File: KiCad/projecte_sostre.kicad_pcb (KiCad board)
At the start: 2 copper layers, 111.2 x 89.4 mm, 149 parts, among them J1 Conn_01x02, J10 DE9_Pins, J11 DE9_Pins, J2 Conn_01x05, J3 Conn_01x02, J4 Conn_01x02, J5 Conn_01x02, J6 Conn_01x02, J7 Screw_Terminal_01x02, J8 Screw_Terminal_01x02, J9 Screw_Terminal_01x02, SW1 SW_Push, SW2 SW_Push, SW3 SW_Push, SW4 SW_Push, SW5 SW_Push, SW6 SW_Push, U1 74AHCT1G125, U10 MCP2561-E-MF, U11 MAX3232, U12 A1101xLH, U13 A1101xLH, U14 L298P, U2 LM393, U3 LM393, U4 PIC24HJ128GP502, U5 LM1117DT-3.3, U6 LM2596T-5, U8 INA219AxD, U9 INA219AxD, Y1 Crystal

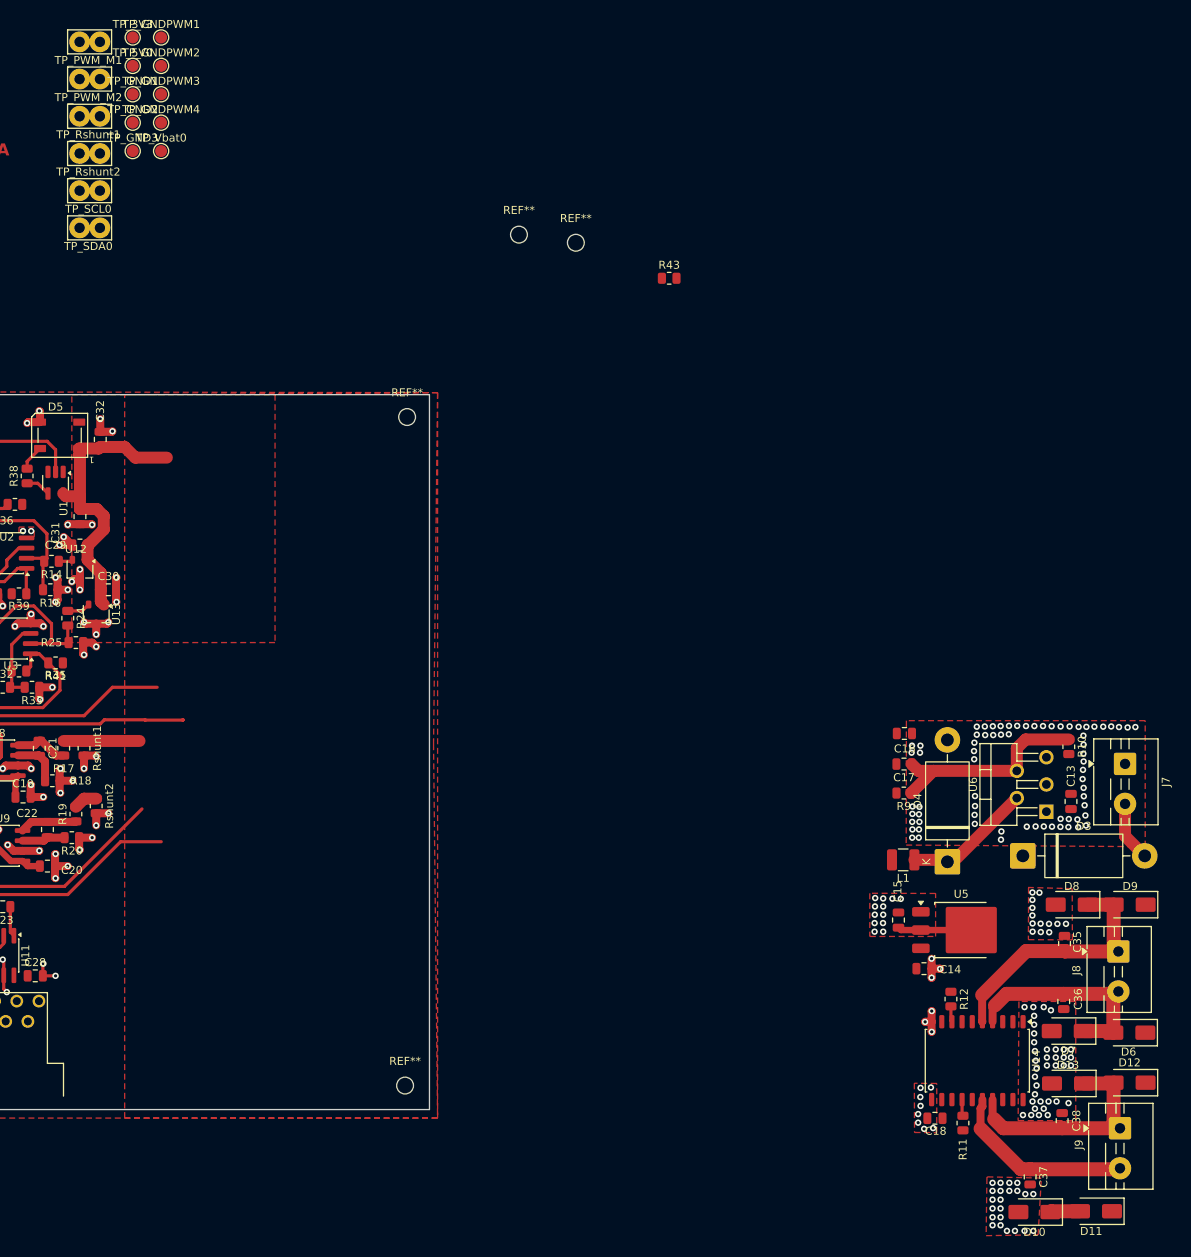
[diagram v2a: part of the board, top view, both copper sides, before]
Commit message: Voy a intentar mejorar el LED, sensor hall / sensor antiatrapamiento
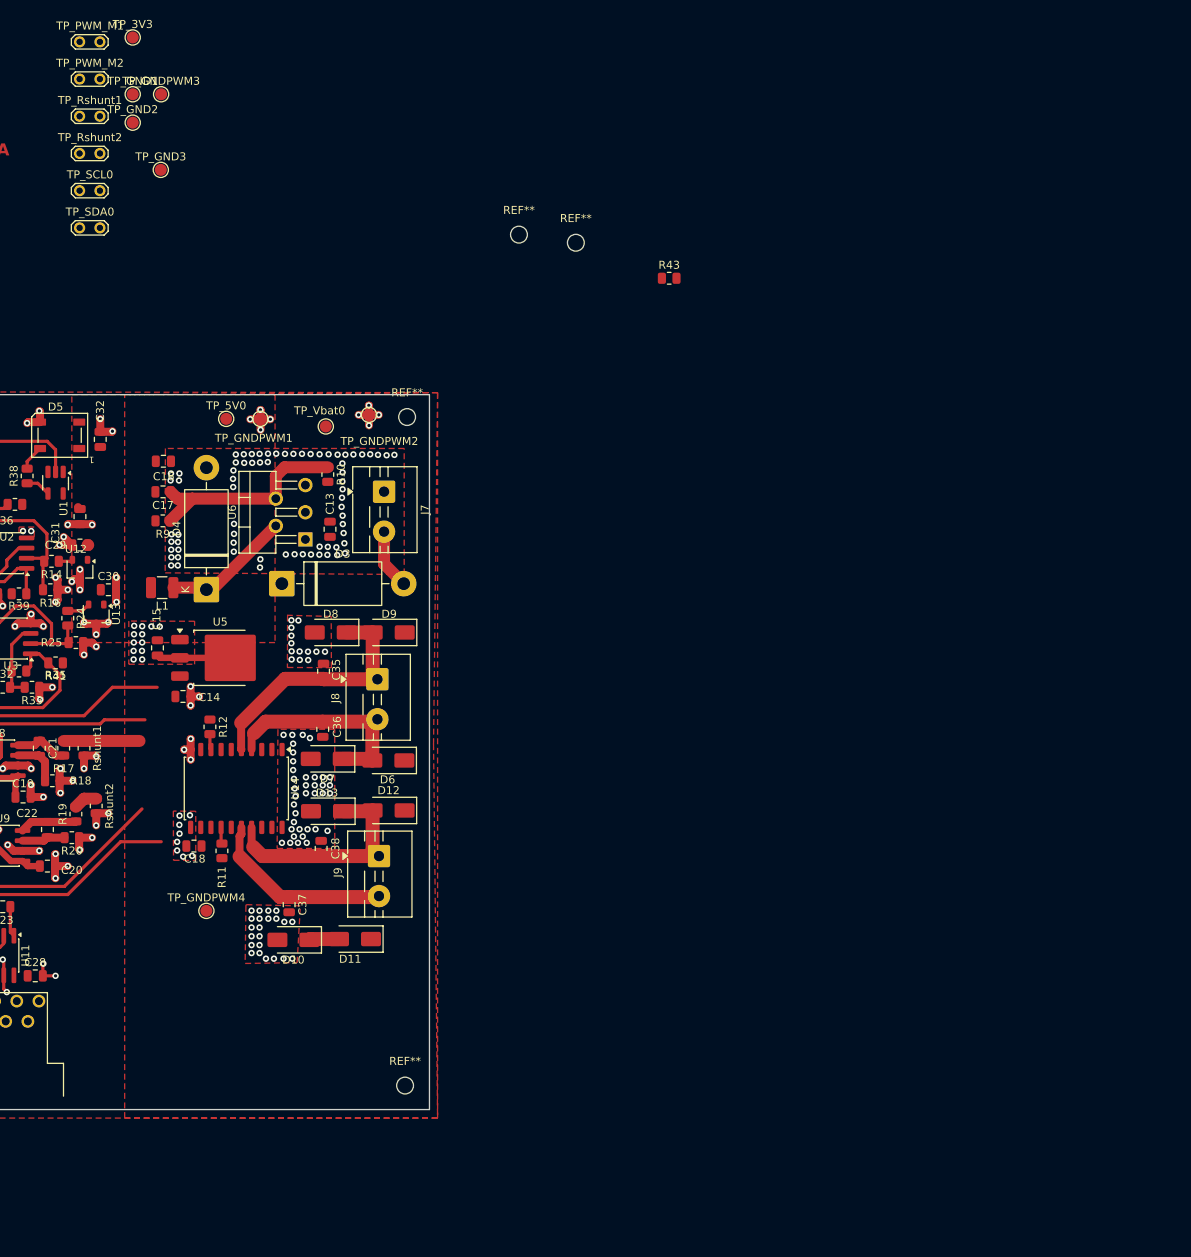
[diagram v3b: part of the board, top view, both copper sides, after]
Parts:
- TP_PWM_M1, TP_PWM_M2, TP_Rshunt1, TP_Rshunt2, TP_SCL0, TP_SDA0: footprint TestPoint:TestPoint_Bridge_Pitch2.54mm_Drill1.3mm -> TestPoint:TestPoint_2Pads_Pitch2.54mm_Drill0.8mm
- moved TP_GNDPWM4 98.7 mm to (213.9, 125.0)
- moved D3 98.7 mm to (223.4, 84.1)
- moved D6 98.7 mm to (236.7, 106.2)
- moved R10 98.7 mm to (229.1, 70.4)
- moved R9 98.7 mm to (208.5, 76.2)
- moved U14 98.7 mm to (217.7, 109.7)
- moved C13 98.7 mm to (229.4, 77.3)
- moved C14 98.7 mm to (211.0, 98.2)
- moved C15 98.7 mm to (207.8, 92.1)
- moved C16 98.7 mm to (208.6, 68.8)
- moved C17 98.7 mm to (208.5, 72.6)
- moved C18 98.7 mm to (212.4, 116.9)
- moved C35 98.7 mm to (228.6, 95.0)
- moved D10 98.7 mm to (224.8, 128.6)
- moved D11 98.7 mm to (232.5, 128.5)
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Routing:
- net 5V: track 37.9 -> 0.43 mm
- net GND: track 154.5 -> 164.6 mm, vias 318 -> 326
- net INA1_M1: track 56.3 -> 51.5 mm

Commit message: ultimos cambios, he puesto abajo sensor anti atrapamiento (usa AVDD y SENSOR_A y _B PROBLEMA porque atraviesa todo una linea muy ancha
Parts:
- moved TP_Rshunt2 110.5 mm to (230.8, 135.8)
- moved TP_Rshunt1 102.7 mm to (209.4, 127.8), turned to 180 degrees
- moved C32 84.8 mm to (281.4, 91.8)
- moved C33 84.8 mm to (267.7, 111.1)
- moved R14 84.8 mm to (275.3, 107.0)
- moved R25 84.8 mm to (278.4, 117.2)
- moved R26 84.8 mm to (264.7, 103.6)
- moved R32 84.8 mm to (269.2, 122.8)
- moved R36 84.8 mm to (270.8, 99.9)
- moved R38 84.8 mm to (272.3, 96.4)
- moved R40 84.8 mm to (264.7, 107.6)
- moved C29 84.8 mm to (278.9, 105.0)
- moved C30 84.8 mm to (282.4, 110.6)
- moved C31 84.8 mm to (278.9, 101.5)
- moved C34 84.8 mm to (266.7, 120.8)
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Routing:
- net SENSE_B: track 2.96 -> 56.4 mm
- net SENSE_A: track 9.48 -> 57.6 mm
- net I2C_SCL: track 70.4 -> 93.1 mm
- net I2C_SDA: track 76.1 -> 97.0 mm
- net GND: track 164.6 -> 182.0 mm, vias 326 -> 366
- net /Analogica/IN+: track 13.9 -> 30.7 mm
- net /Analogica/IN-: track 11.6 -> 23.3 mm
- net INB2_M2: track 58.8 -> 51.0 mm, vias 0 -> 2
- net M2_OUT1: track 27.1 -> 34.2 mm
- net AVDD: track 59.1 -> 66.0 mm, vias 0 -> 2
- net INB1_M2: track 61.9 -> 62.7 mm, vias 0 -> 2
- added copper zone on F.Cu, net AVDD
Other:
- board text added: "mirar TEMA 3V3 y pq no llega, hacer que llegue poniendo algo"

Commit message: Sensor Hall y LED mas o menos definitivos
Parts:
- moved R39 102.1 mm to (175.0, 77.2)
- moved R33 91.8 mm to (189.3, 84.8)
- moved R32 91.7 mm to (185.9, 84.5)
- moved U2 89.8 mm to (184.2, 78.8), turned to 0 degrees
- moved R42 89.8 mm to (179.2, 88.4), turned to -90 degrees
- moved R30 88.4 mm to (175.0, 79.7)
- moved R34 87.8 mm to (179.1, 77.9), turned to 90 degrees
- moved R25 87.4 mm to (194.7, 92.2)
- moved C33 87.3 mm to (188.3, 74.9)
- moved R24 87.2 mm to (193.8, 89.1)
- moved R14 87.1 mm to (193.7, 76.7), turned to -90 degrees
- moved C34 87.1 mm to (184.2, 92.7)
- moved U3 87.1 mm to (187.8, 88.8)
- moved U12 86.8 mm to (197.9, 76.8)
- moved R16 86.6 mm to (194.3, 79.5)
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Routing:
- net GND: track 182.0 -> 88.2 mm, vias 366 -> 381
- net AVDD: track 66.0 -> 39.0 mm
- net LED_RGB: track 72.9 -> 46.9 mm
- net HIGH_UP_M1_Pos_Max: track 69.5 -> 45.8 mm
- net I2C_SDA: track 97.0 -> 75.6 mm
- net /Digital/VOUT_Hall2: track 31.6 -> 15.5 mm
- net DOWN_LOW_M1_Pos_Min: track 49.6 -> 34.4 mm, vias 0 -> 2
- net I2C_SCL: track 93.1 -> 78.1 mm, vias 4 -> 2
- net DOWN_LOW_M1_Pos_Max: track 41.6 -> 27.4 mm
- net /Analogica/IN+: track 30.7 -> 16.8 mm
- net /Analogica/IN-: track 23.3 -> 11.7 mm
- net SENSE_A: track 57.6 -> 48.1 mm
- net INB1_M2: track 62.7 -> 53.3 mm
- net /Digital/Vref_1V_Max: track 18.0 -> 8.88 mm
- net +3.3V: track 14.5 -> 21.0 mm
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
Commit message: Layout con pocos cables en capa Bot pero todavai hay que hacer cambios que nos dijo el Miercoles pasado
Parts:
- removed TP_GNDPWM3: TestPoint, TestPoint:TestPoint_Pad_D1.5mm
- R43: moved to B.Cu
- moved REF** 184.2 mm to (108.3, 145.8)
- moved REF** 146.1 mm to (108.2, 60.0)
- moved TP_SDA0 110.4 mm to (157.7, 142.4)
- moved TP_SCL0 109.3 mm to (157.7, 136.5)
- moved TP_GND2 101.8 mm to (140.1, 105.1)
- moved R43 97.9 mm to (185.4, 92.1), turned to -90 degrees
- moved TP_PWM_M2 86.5 mm to (178.3, 105.2)
- moved TP_3V3 86.0 mm to (139.0, 71.3)
- moved TP_PWM_M1 85.3 mm to (167.9, 96.1)
- moved TP_GND1 84.5 mm to (135.5, 71.4)
- moved J5 78.4 mm to (109.0, 94.5)
- moved J3 74.4 mm to (109.0, 74.2), turned to 0 degrees
- moved SW4 73.1 mm to (112.5, 88.5), turned to 90 degrees
- moved J6 73.0 mm to (109.1, 104.7), turned to 0 degrees
- moved SW5 72.4 mm to (112.6, 98.5), turned to 90 degrees
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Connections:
- TP_PWM_M1 pad 1: INA1_M1 -> INA2_M1
- U4 pad 10: INB1_M2 -> CAN_TX
- U4 pad 11: INB2_M2 -> STBY_Trans_CAN
- U4 pad 14: unconnected-(U4-RB14-Pad14) -> USART_TX
- U4 pad 15: unconnected-(U4-RB15-Pad15) -> USART_RX
- U4 pad 2: unconnected-(U4-RC6-Pad2) -> /Microprocesador/M1_go_Max
- U4 pad 23: INA1_M1 -> uC_programado?
- U4 pad 24: INA2_M1 -> unconnected-(U4-RB3-Pad24)
- U4 pad 25: DOWN_LOW_M1_Pos_Min -> unconnected-(U4-RC0-Pad25)
- U4 pad 26: HIGH_UP_M1_Pos_Min -> INB1_M2
- U4 pad 27: DOWN_LOW_M1_Pos_Max -> INB2_M2
- U4 pad 3: uC_programado? -> /Microprocesador/M1_go_Min
- U4 pad 32: HIGH_UP_M1_Pos_Max -> INA1_M1
- U4 pad 33: LED_RGB -> INA2_M1
- U4 pad 34: STBY_Trans_CAN -> DOWN_LOW_M1_Pos_Min
- U4 pad 35: ON/OFF_LED -> HIGH_UP_M1_Pos_Min
- U4 pad 36: CAN_RX -> unconnected-(U4-RC3-Pad36)
- U4 pad 37: CAN_TX -> unconnected-(U4-RC4-Pad37)
- U4 pad 38: /Microprocesador/M1_go_Max -> unconnected-(U4-RC5-Pad38)
- U4 pad 4: unconnected-(U4-RC8-Pad4) -> /Microprocesador/M2_go_Max
- U4 pad 41: /Microprocesador/M1_go_Min -> DOWN_LOW_M1_Pos_Max
- U4 pad 42: /Microprocesador/M2_go_Max -> HIGH_UP_M1_Pos_Max
- U4 pad 43: /Microprocesador/M2_go_Min -> LED_RGB
- U4 pad 5: unconnected-(U4-RC9-Pad5) -> /Microprocesador/M2_go_Min
- U4 pad 8: USART_TX -> ON/OFF_LED
- U4 pad 9: USART_RX -> CAN_RX
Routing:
- net I2C_SDA: track 75.6 -> 131.3 mm, vias 2 -> 4
- net I2C_SCL: track 78.1 -> 130.0 mm, vias 2 -> 4
- net /Microprocesador/M1_go_Max: track 15.7 -> 63.2 mm, vias 1 -> 0
- net +3.3V: track 21.0 -> 68.0 mm, vias 0 -> 14
- net /Microprocesador/M1_go_Min: track 14.1 -> 56.2 mm
- net AVDD: track 39.0 -> 77.4 mm, vias 2 -> 6
- net (no net): track 36.8 -> 0.00 mm
- net STBY_Trans_CAN: track 4.18 -> 40.2 mm, vias 1 -> 0
- net CAN_TX: track 3.05 -> 32.5 mm
- net LED_RGB: track 46.9 -> 76.2 mm
- net CAN_RX: track 2.83 -> 30.6 mm
- net HIGH_UP_M1_Pos_Min: track 6.24 -> 27.0 mm
- net ON/OFF_LED: track 20.2 -> 40.9 mm, vias 1 -> 0
- net DOWN_LOW_M1_Pos_Max: track 27.4 -> 45.7 mm
- net INA2_M1: track 52.2 -> 33.9 mm
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- added copper zone on B.Cu, net GND
- removed copper zone on F.Cu, net (none)
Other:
- board size 111.2 x 89.4 mm -> 111.8 x 92.1 mm
- board text added: "Fet per: Marc Baillo i Nabel Khrourouch"
- board text removed: "3V3 o 5V"
- board text removed: "ACORDARSE PONER TEST EN LA PCB"
- board text removed: "GND Power"
- board text removed: "GND normal"
- board text removed: "mirar TEMA 3V3 y pq no llega, hacer que llegue poniendo algo"
- board text removed: "señales digitales"

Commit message: Cambios Layout propuestos para mejorar posicionamiento
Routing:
- net +3.3V: track 68.0 -> 57.2 mm
- net GND: track 83.1 -> 79.0 mm
- net AVDD: track 77.4 -> 78.8 mm, vias 6 -> 7

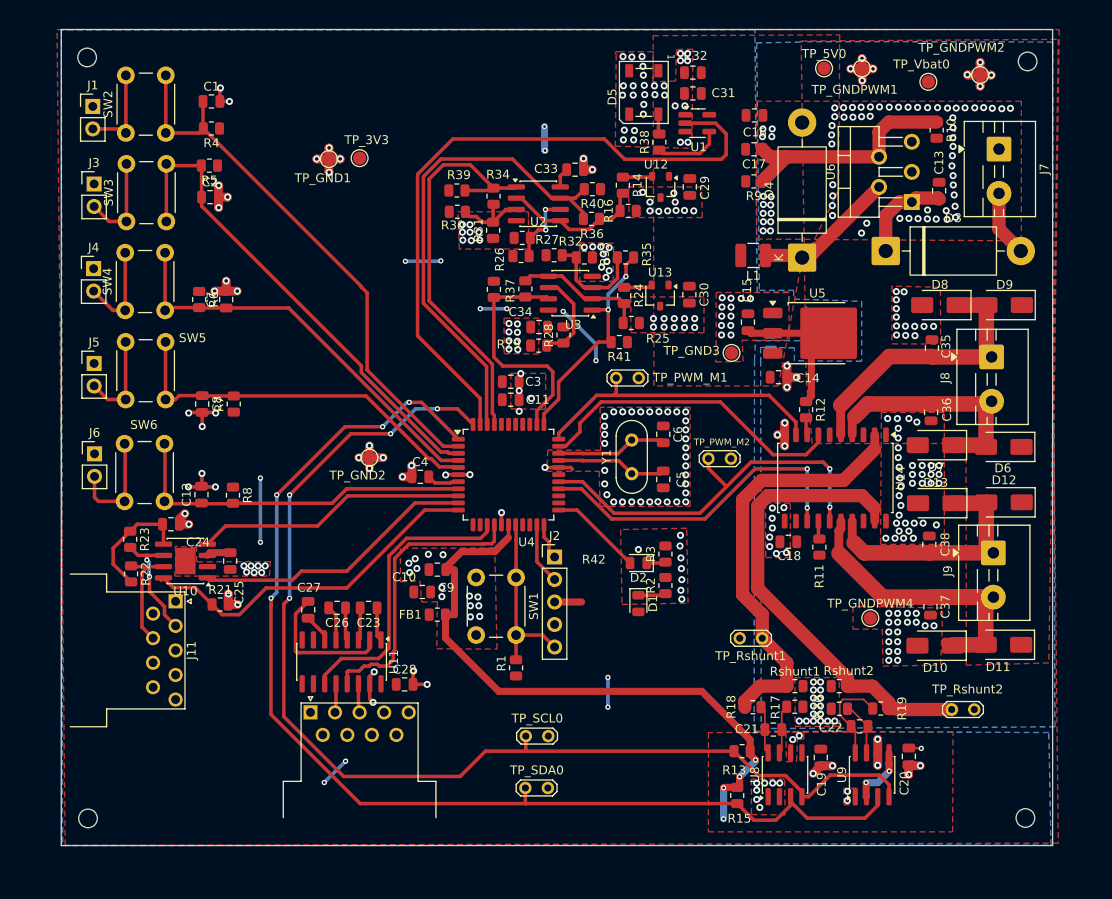
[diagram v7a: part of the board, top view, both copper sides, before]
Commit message: Arreglo de algunos fallos DRC
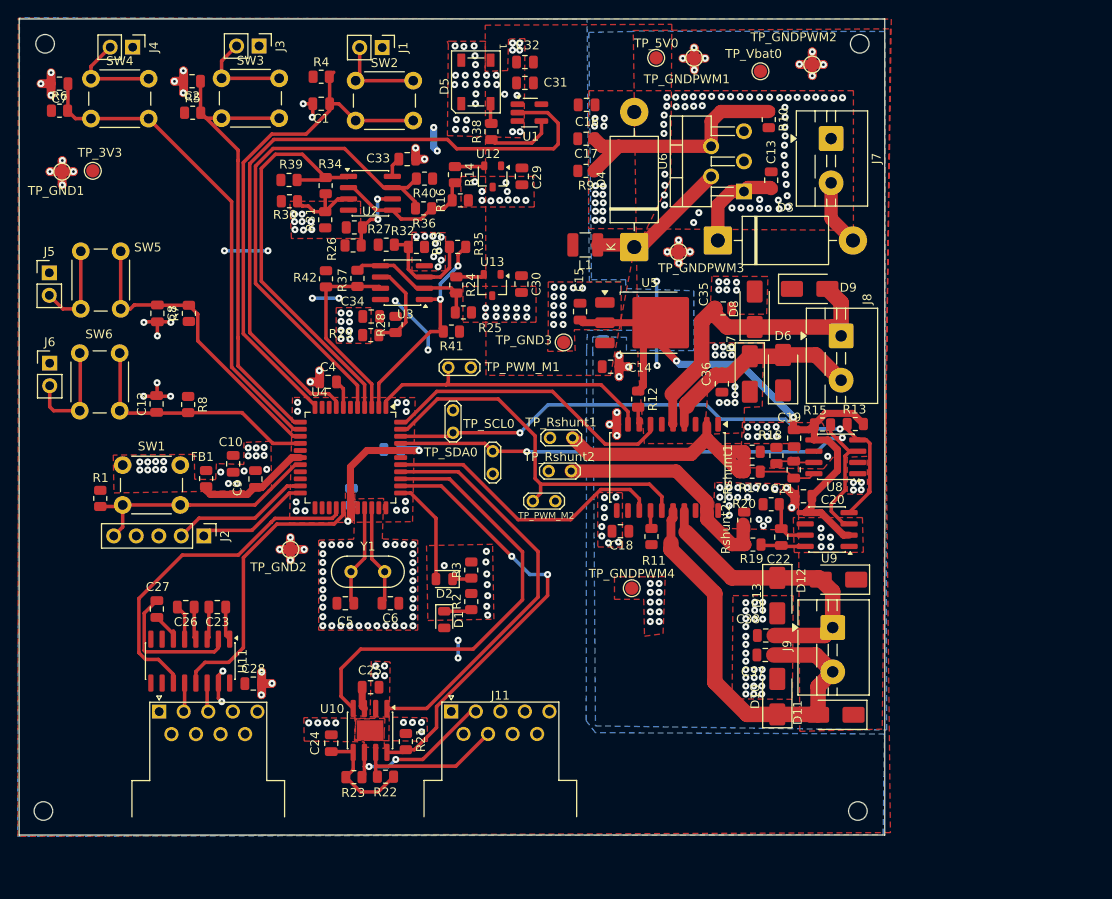
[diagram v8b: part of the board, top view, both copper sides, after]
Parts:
- added TP_GNDPWM3: TestPoint, TestPoint:TestPoint_Pad_D1.5mm, F.Cu at (175.0, 81.9)
- C11, C3: moved to B.Cu
- moved TP_Rshunt2 50.7 mm to (162.9, 106.6), turned to 180 degrees
- moved R1 50.7 mm to (109.7, 109.7), turned to -90 degrees
- moved R15 42.9 mm to (191.2, 101.4), turned to 0 degrees
- moved J2 39.6 mm to (121.4, 113.9), turned to -90 degrees
- moved R13 39.1 mm to (194.9, 101.3)
- moved SW1 38.7 mm to (118.8, 110.4), turned to 180 degrees
- moved C5 38.5 mm to (137.4, 121.5), turned to 0 degrees
- moved TP_SDA0 38.2 mm to (154.0, 104.4), turned to -90 degrees
- moved R23 36.8 mm to (138.3, 141.1), turned to 0 degrees
- moved R22 36.7 mm to (141.9, 141.1), turned to 0 degrees
- moved U8 36.3 mm to (192.7, 105.0), turned to 180 degrees
- moved C6 36.2 mm to (142.5, 121.5), turned to 180 degrees
- moved C19 36.1 mm to (188.0, 102.9)
- moved TP_SCL0 35.2 mm to (149.5, 102.3), turned to 90 degrees
- moved Y1 33.5 mm to (138.0, 118.0), turned to 0 degrees
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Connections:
- net Net-(D1-K) renamed /Microprocesador/entre_D1_R2
- net Net-(D2-K) renamed /Microprocesador/entre_D2_R3
- net Net-(U11-C1+) renamed /Digital/C1+
- net Net-(U11-C1-) renamed /Digital/C1-
- net Net-(U11-C2+) renamed /Digital/C2+
- net Net-(U11-C2-) renamed /Digital/C2-
- net Net-(U11-VS+) renamed /Digital/VS+
- net Net-(U11-VS-) renamed /Digital/VS-
- C1 pad 1: /Microprocesador/M1_go_Max -> M1_go_Max
- C19 pad 1: AVDD -> +3.3V
- C2 pad 1: /Microprocesador/M1_go_Min -> M1_go_Min
- C20 pad 1: AVDD -> +3.3V
- C7 pad 1: /Microprocesador/M2_go_Max -> M2_go_Max
- C8 pad 1: /Microprocesador/M2_go_Min -> M2_go_Min
- C9 pad 1: AVDD -> /Microprocesador/AVDD
- FB1 pad 2: AVDD -> /Microprocesador/AVDD
- R13 pad 1: AVDD -> +3.3V
- R15 pad 1: AVDD -> +3.3V
- R4 pad 2: /Microprocesador/M1_go_Max -> M1_go_Max
- R5 pad 2: /Microprocesador/M1_go_Min -> M1_go_Min
- R6 pad 2: /Microprocesador/M2_go_Max -> M2_go_Max
- R7 pad 2: /Microprocesador/M2_go_Min -> M2_go_Min
- SW2 pad 2: /Microprocesador/M1_go_Max -> M1_go_Max
- SW3 pad 2: /Microprocesador/M1_go_Min -> M1_go_Min
- SW4 pad 2: /Microprocesador/M2_go_Max -> M2_go_Max
- SW5 pad 2: /Microprocesador/M2_go_Min -> M2_go_Min
- U4 pad 1: I2C_SDA -> INA2_M1
- U4 pad 10: CAN_TX -> unconnected-(U4-RB12-Pad10)
- U4 pad 11: STBY_Trans_CAN -> M1_go_Max
- U4 pad 12: unconnected-(U4-RA10-Pad12) -> M1_go_Min
- U4 pad 13: unconnected-(U4-RA7-Pad13) -> M2_go_Max
- U4 pad 14: USART_TX -> M2_go_Min
- U4 pad 15: USART_RX -> ON/OFF_LED
- U4 pad 17: AVDD -> /Microprocesador/AVDD
- U4 pad 2: /Microprocesador/M1_go_Max -> DOWN_LOW_M1_Pos_Min
- U4 pad 23: uC_programado? -> unconnected-(U4-RB2-Pad23)
- U4 pad 26: INB1_M2 -> USART_TX
- U4 pad 27: INB2_M2 -> USART_RX
- U4 pad 3: /Microprocesador/M1_go_Min -> HIGH_UP_M1_Pos_Min
- U4 pad 32: INA1_M1 -> unconnected-(U4-RA8-Pad32)
- U4 pad 33: INA2_M1 -> unconnected-(U4-RB4-Pad33)
- U4 pad 34: DOWN_LOW_M1_Pos_Min -> uC_programado?
- U4 pad 35: HIGH_UP_M1_Pos_Min -> STBY_Trans_CAN
- U4 pad 36: unconnected-(U4-RC3-Pad36) -> CAN_RX
- U4 pad 37: unconnected-(U4-RC4-Pad37) -> CAN_TX
- U4 pad 38: unconnected-(U4-RC5-Pad38) -> INB1_M2
- U4 pad 4: /Microprocesador/M2_go_Max -> DOWN_LOW_M1_Pos_Max
- U4 pad 41: DOWN_LOW_M1_Pos_Max -> I2C_SDA
- U4 pad 42: HIGH_UP_M1_Pos_Max -> I2C_SCL
- U4 pad 43: LED_RGB -> INB2_M2
- U4 pad 44: I2C_SCL -> INA1_M1
- U4 pad 5: /Microprocesador/M2_go_Min -> HIGH_UP_M1_Pos_Max
- U4 pad 8: ON/OFF_LED -> LED_RGB
- U4 pad 9: CAN_RX -> unconnected-(U4-PGEC2/RB11-Pad9)
- U8 pad 5: AVDD -> +3.3V
- U9 pad 2: AVDD -> +3.3V
- U9 pad 5: AVDD -> +3.3V
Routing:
- net AVDD: track 78.8 -> 0.00 mm, vias 7 -> 0
- net I2C_SDA: track 131.3 -> 67.2 mm, vias 4 -> 2
- net I2C_SCL: track 130.0 -> 66.0 mm, vias 4 -> 2
- net /Microprocesador/M1_go_Max: track 62.8 -> 0.00 mm
- net M1_go_Max: track 0.00 -> 57.9 mm
- net +3.3V: track 57.2 -> 115.0 mm
- net /Microprocesador/M1_go_Min: track 56.1 -> 0.00 mm
- net M2_go_Max: track 0.00 -> 55.6 mm
- net M1_go_Min: track 0.00 -> 53.5 mm
- net /Microprocesador/M2_go_Max: track 46.8 -> 0.00 mm
- net /Microprocesador/M2_go_Min: track 43.1 -> 0.00 mm
- net M2_go_Min: track 0.00 -> 34.8 mm
- net SENSE_B: track 53.5 -> 26.6 mm
- net CAN_RX: track 30.6 -> 51.3 mm
- net SENSE_A: track 48.1 -> 29.0 mm
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- removed copper zone on F.Cu, net AVDD
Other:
- board size 111.8 x 92.1 mm -> 97.6 x 92.1 mm
